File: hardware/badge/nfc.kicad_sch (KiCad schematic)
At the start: 56 parts, among them J1001 Conn_01x01_Female, J1002 Conn_01x01_Female, J1003 Conn_01x01_Female, J1004 Conn_01x01_Female, J1005 Conn_01x01_Female, J1006 Conn_01x01_Female, J1007 Conn_01x01_Female, J1008 Conn_01x01_Female, P1001 U.FL-R-SMT-1_10_, P1002 U.FL-R-SMT-1_10_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

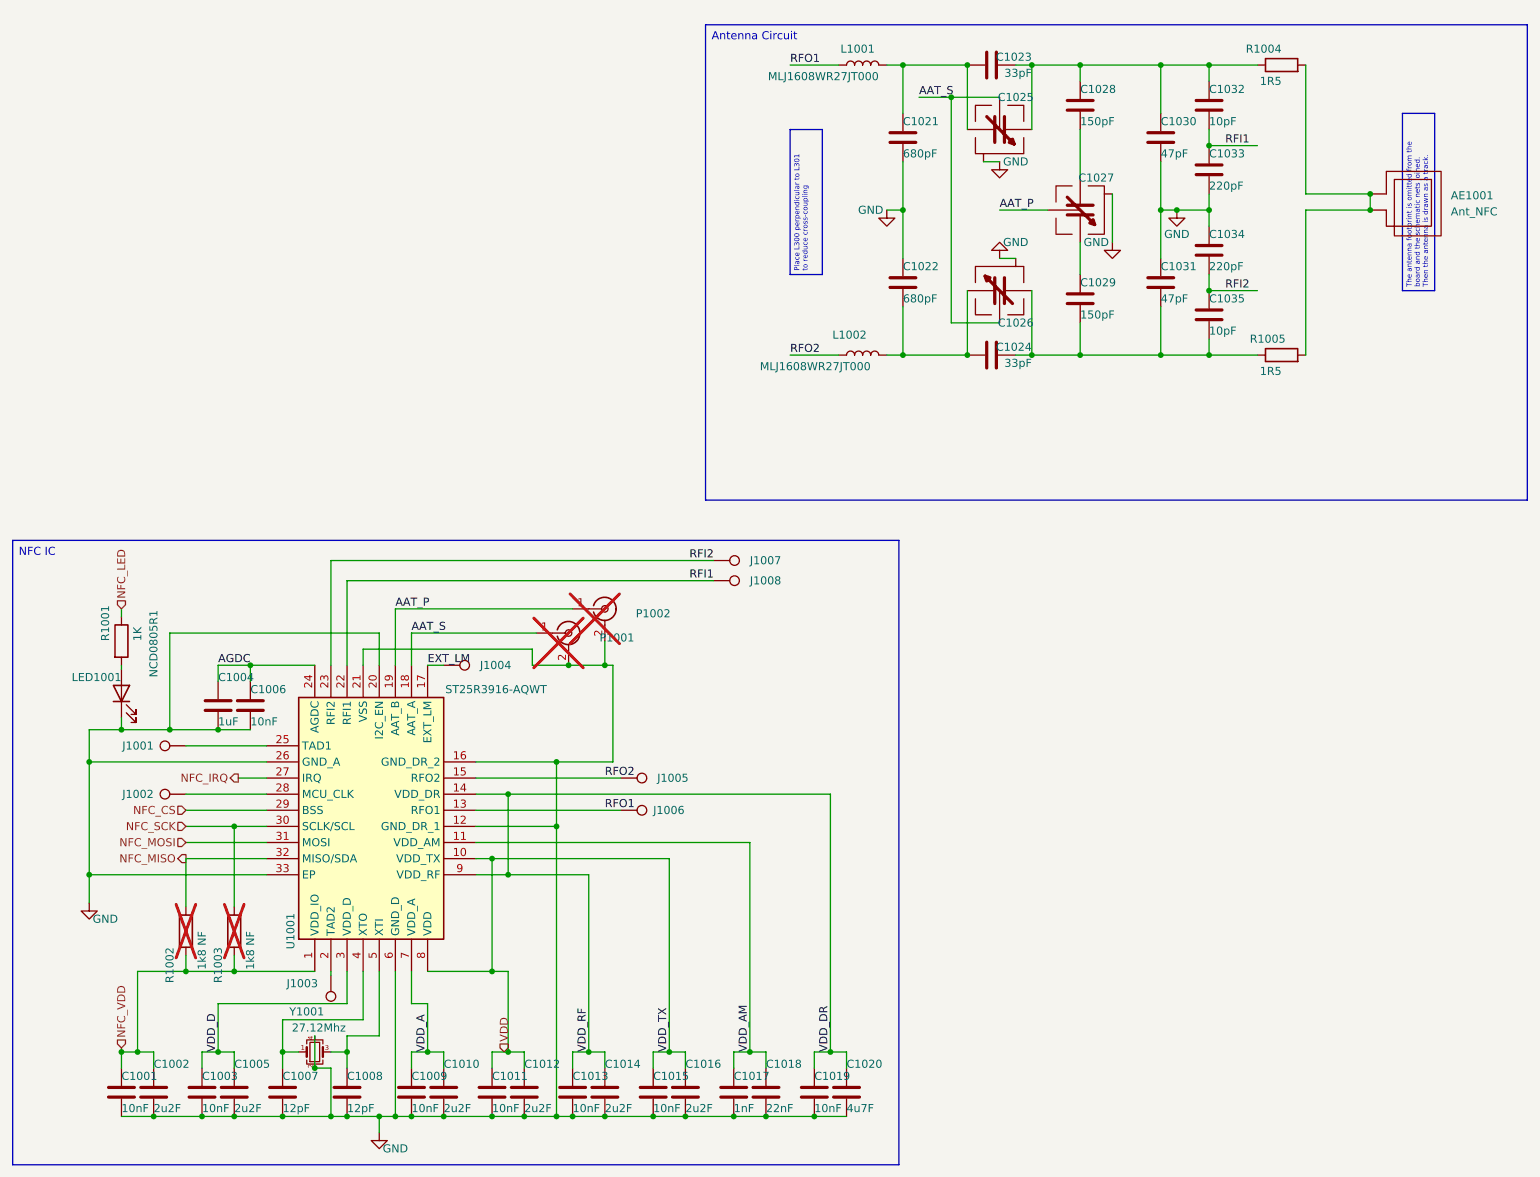
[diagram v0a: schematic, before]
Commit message: feat: badge v2 PCB design with panelization support
Updated schematic and PCB layout for badge v2 revision. Added
panelization project with JLCPCB production files, panelize script,
and board SVG artwork.
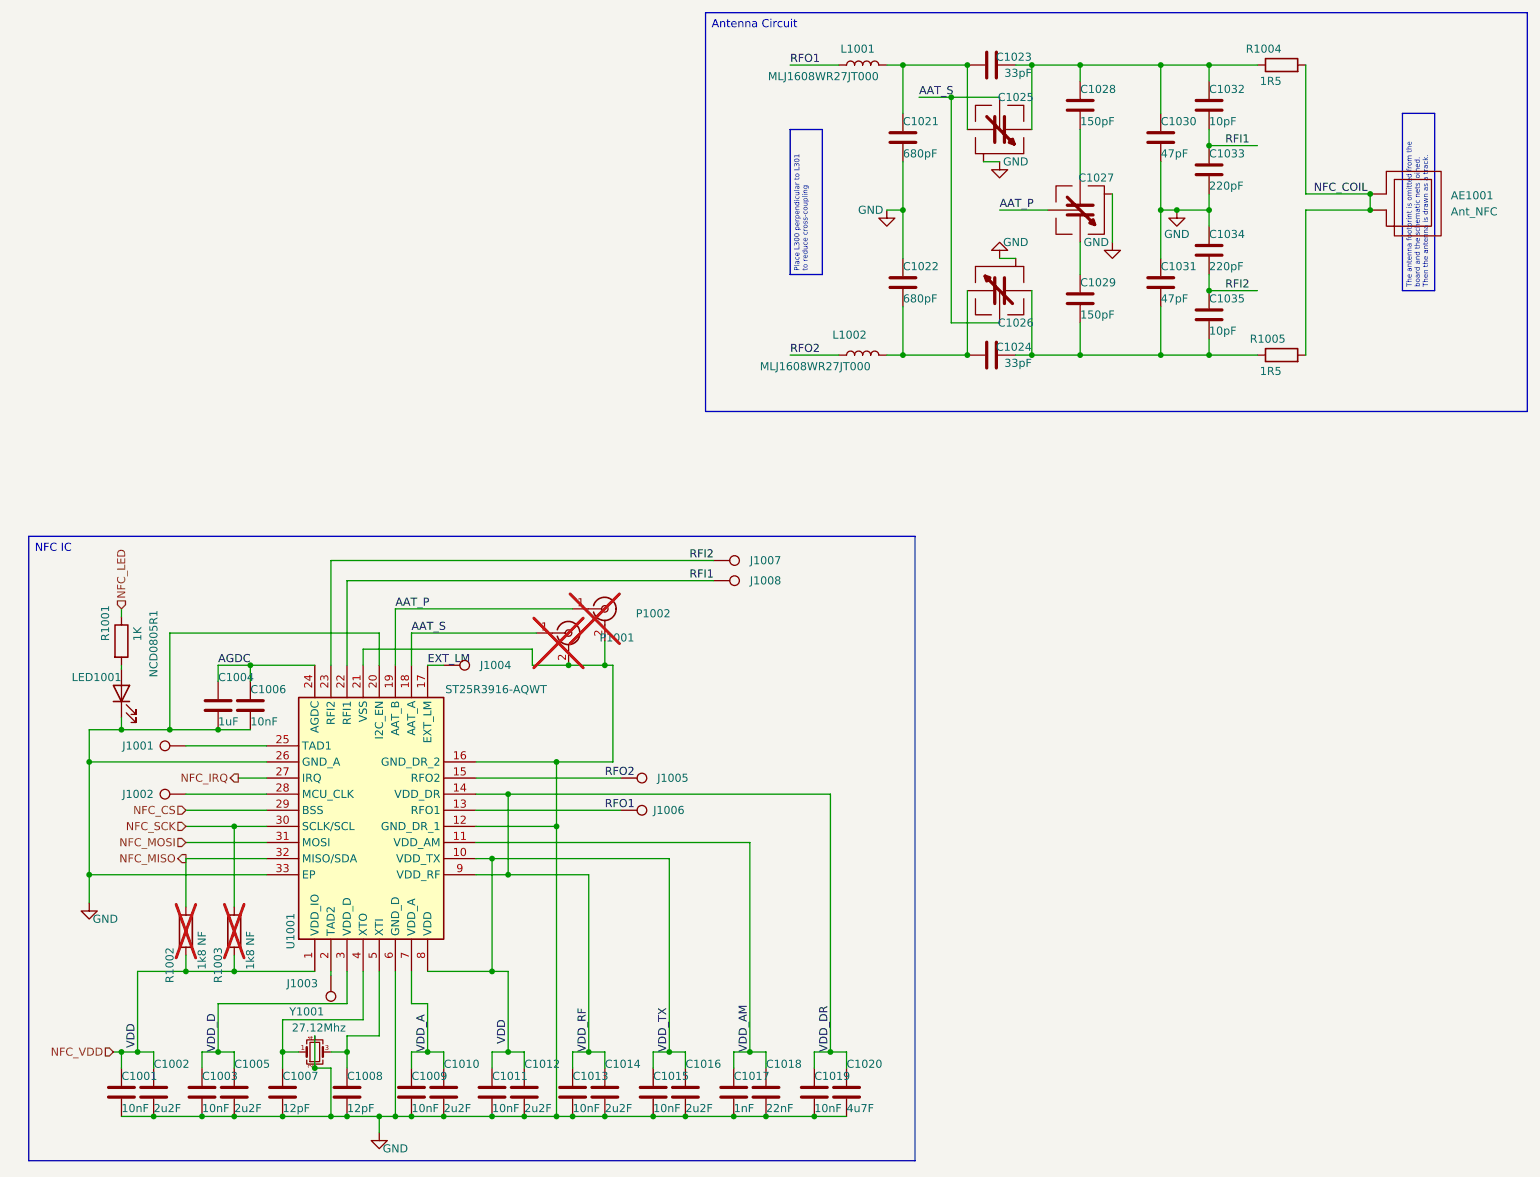
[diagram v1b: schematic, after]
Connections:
- net VDD is gone; now on net NFC_VDD: C1011.1, C1012.1, C1015.1, C1016.1, U1001.10 (VDD_TX), U1001.8 (VDD)
- net NFC_COIL: now reaches AE1001.1, R1004.2, R1005.2
